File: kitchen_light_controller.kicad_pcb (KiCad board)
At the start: 2 copper layers, 48 x 57 mm, 9 parts, among them J1 1935161, J2 1935161, J3 1935161, J4 1935161, J5 1935161, U1 SC0915, U2 VND7140AJTR, U3 VND7140AJTR

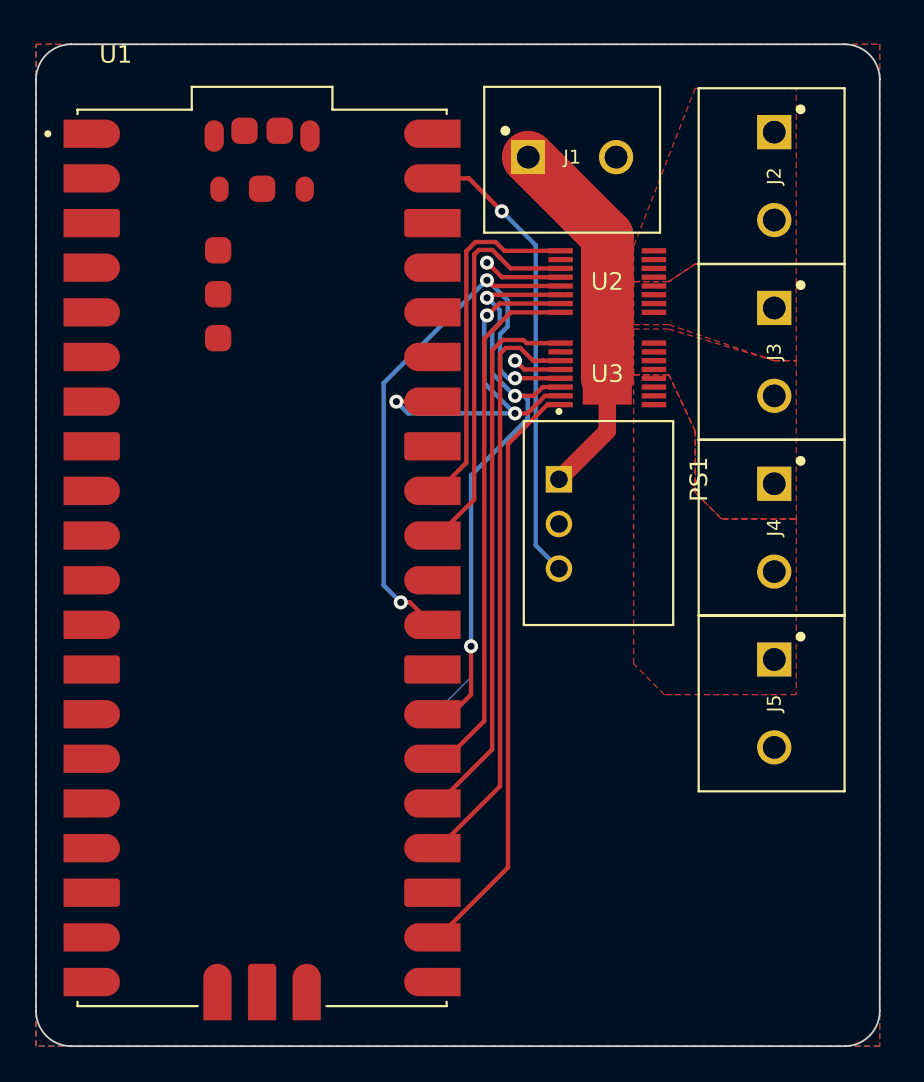
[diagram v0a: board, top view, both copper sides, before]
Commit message: Reduced to dual channel (Single IC)
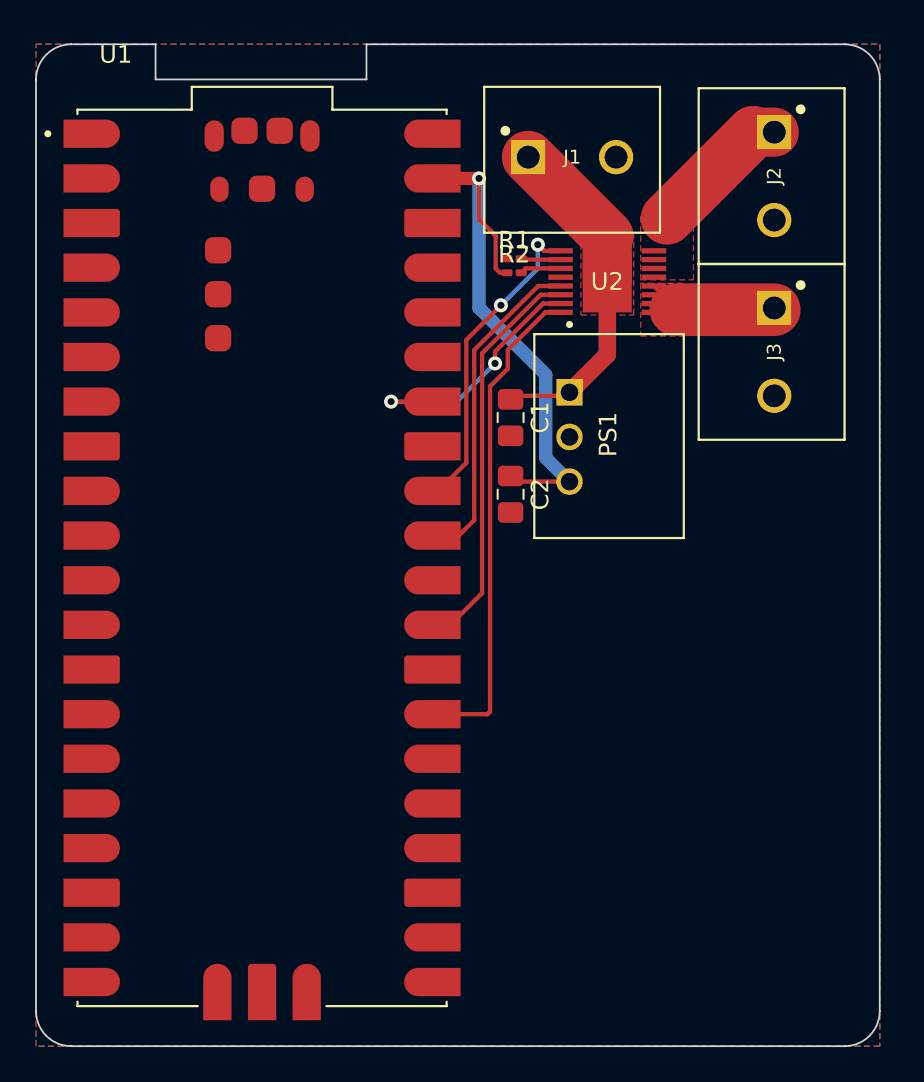
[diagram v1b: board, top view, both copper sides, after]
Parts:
- removed J4, J5: 1935161, Raspberry Pi Pico:PHOENIX_1935161
- removed U3: VND7140AJTR, Raspberry Pi Pico:POWERSSO16_STM
- added C1: 10μF, Capacitor_SMD:C_0805_2012Metric_Pad1.18x1.45mm_HandSolder, F.Cu at (103.0, 50.2)
- added C2: 10μF, Capacitor_SMD:C_0805_2012Metric_Pad1.18x1.45mm_HandSolder, F.Cu at (103.0, 54.6)
- added R1: 15KΩ, Resistor_SMD:R_0201_0603Metric_Pad0.64x0.40mm_HandSolder, F.Cu at (103.2, 41.2)
- added R2: 15KΩ, Resistor_SMD:R_0201_0603Metric_Pad0.64x0.40mm_HandSolder, F.Cu at (103.2, 42.0)
- moved PS1 4.99 mm to (108.6, 51.3)
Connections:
- U1 pad 22: PWM3 -> unconnected-(U1-GP17-Pad22)
- U1 pad 24: MS_CE1 -> unconnected-(U1-GP18-Pad24)
- U1 pad 25: PWM2 -> unconnected-(U1-GP19-Pad25)
- U1 pad 26: PWM1 -> unconnected-(U1-GP20-Pad26)
- U1 pad 27: MS_SEL1 -> PWM1
- U1 pad 29: MS_SEL0 -> MS_SEL1
- U1 pad 31: MS_CE0 -> MS_SEL0
- U2 pad 2: unconnected-(U2-*FAULTRST-Pad2) -> Net-(U2-*FAULTRST)
- U2 pad 3: MS_CE0 -> Net-(U2-SEN)
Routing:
- net PWM3: track 34.0 -> 0.00 mm
- net MS_CE1: track 33.8 -> 0.00 mm
- net PWM2: track 31.6 -> 0.00 mm
- net MS_CE0: track 22.6 -> 0.00 mm
- net MS_SEL0: track 37.3 -> 18.8 mm, vias 3 -> 0
- net MS_SEL1: track 40.1 -> 23.1 mm, vias 3 -> 0
- net MULTISENSE: track 23.0 -> 14.7 mm, vias 3 -> 2
- net Net-(J2-Pad1): track 0.00 -> 8.13 mm
- net 3.3V: track 26.4 -> 34.4 mm
- net Net-(J3-Pad1): track 0.00 -> 7.36 mm
- net GND: track 7.34 -> 0.00 mm, vias 2 -> 0
- net VIN: track 22.3 -> 19.7 mm
- net Net-(U2-SEN): track 0.00 -> 2.34 mm
- net PWM1: track 30.6 -> 28.2 mm
- net PWM0: track 20.4 -> 18.1 mm, vias 0 -> 2
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- added copper zone on F.Cu, net VIN
- removed copper zone on F.Cu, net Net-(J4-Pad1)
- removed copper zone on F.Cu, net Net-(J5-Pad1)
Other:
- outline, holes or cut-outs redrawn

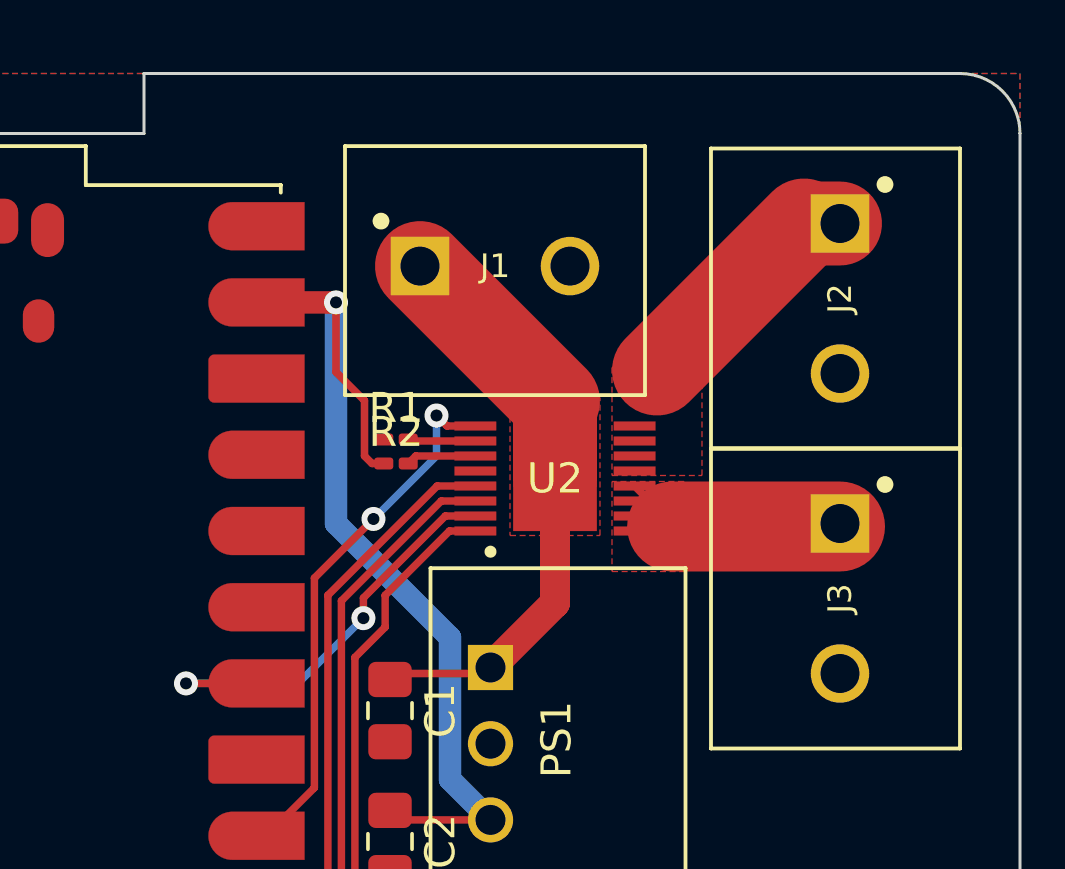
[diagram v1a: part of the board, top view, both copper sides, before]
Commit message: Reinforced current carrying traces with vias
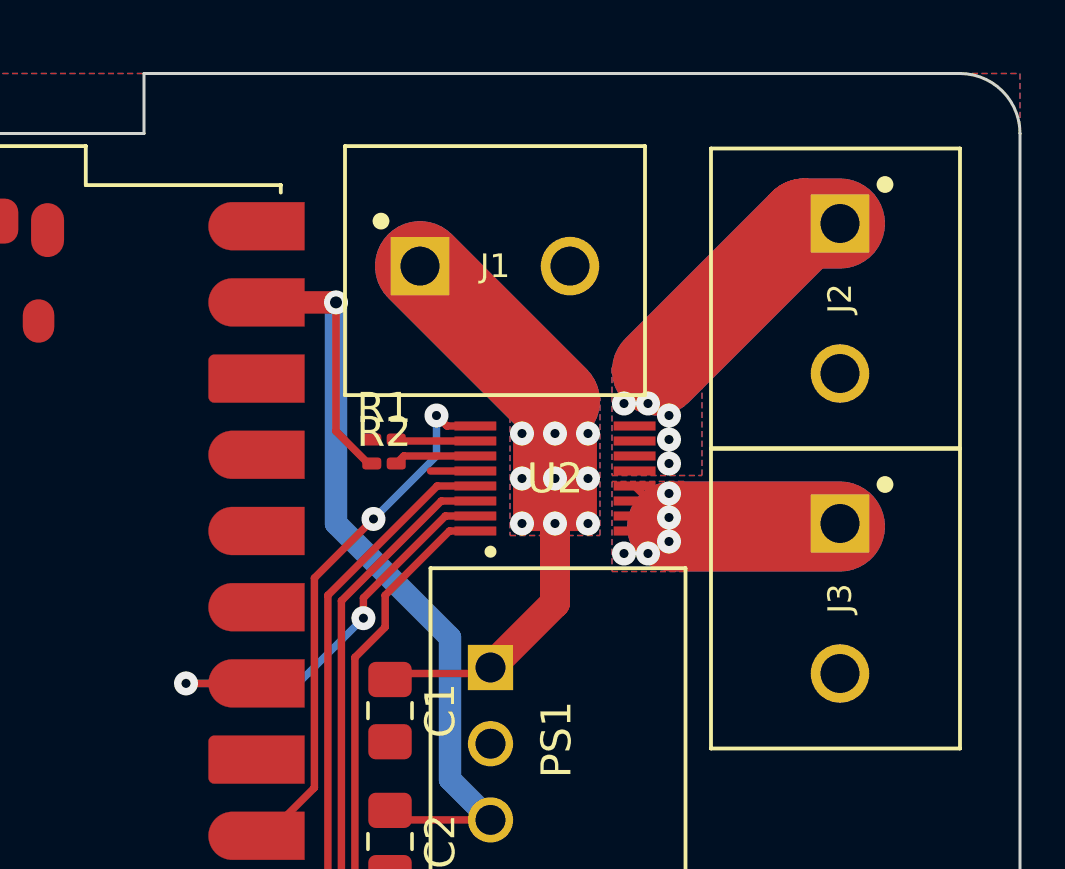
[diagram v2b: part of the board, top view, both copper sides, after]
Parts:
- moved R1 0.40 mm to (102.8, 41.2)
- moved R2 0.40 mm to (102.8, 42.0)
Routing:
- net Net-(J2-Pad1): track 8.13 -> 16.3 mm, vias 0 -> 5
- net Net-(J3-Pad1): track 7.36 -> 13.0 mm, vias 0 -> 5
- net VIN: track 19.7 -> 23.4 mm, vias 0 -> 9
- net GND: track 0.00 -> 1.50 mm
- added copper zone on B.Cu, net Net-(J2-Pad1)
- added copper zone on B.Cu, net Net-(J3-Pad1)
- added copper zone on B.Cu, net VIN
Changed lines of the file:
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@@
   (net 49 "MULTISENSE")
   (footprint "Resistor_SMD:R_0201_0603Metric_Pad0.64x0.40mm_HandSolder" (layer "F.Cu")
-    (at 103.2 41.2)
+    (at 102.8 41.2)
     (descr "Resistor SMD 0201 (0603 Metric), square (rectangular) end terminal, IPC_7351 nominal with elongated pad for handsoldering. (Body size source: https://www.vishay.com/docs/20052/crcw0201e3.pdf), generated with kicad-footprint-generator")
     (tags "resistor handsolder")
@@
   )
   (footprint "Resistor_SMD:R_0201_0603Metric_Pad0.64x0.40mm_HandSolder" (layer "F.Cu")
-    (at 103.2 42)
+    (at 102.8 42)
     (descr "Resistor SMD 0201 (0603 Metric), square (rectangular) end terminal, IPC_7351 nominal with elongated pad for handsoldering. (Body size source: https://www.vishay.com/docs/20052/crcw0201e3.pdf), generated with kicad-footprint-generator")
     (tags "resistor handsolder")
@@
   (segment (start 103 49.2) (end 103.2 49) (width 0.25) (layer "F.Cu") (net 1))
   (segment (start 103.2 49) (end 106.15 49) (width 0.25) (layer "F.Cu") (net 1))
-  (segment (start 108.5 39.92) (end 108.5 42.5) (width 2.8) (layer "F.Cu") (net 1))
   (segment (start 108.5 46.65) (end 108.5 42.5) (width 1) (layer "F.Cu") (net 1))
   (segment (start 104 35.42) (end 108.5 39.92) (width 3) (layer "F.Cu") (net 1))
   (segment (start 106.15 49) (end 106.35 48.8) (width 0.25) (layer "F.Cu") (net 1))
   (segment (start 106.35 48.8) (end 108.5 46.65) (width 1) (layer "F.Cu") (net 1))
-  (segment (start 118 34) (end 116.8 34) (width 2.8) (layer "F.Cu") (net 3))
+  (via (at 107.4 42.5) (size 0.8) (drill 0.3) (layers "F.Cu" "B.Cu") (net 1))
+  (via (at 109.6 42.5) (size 0.8) (drill 0.3) (layers "F.Cu" "B.Cu") (net 1))
+  (via (at 109.6 41) (size 0.8) (drill 0.3) (layers "F.Cu" "B.Cu") (net 1))
+  (via (at 108.5 41) (size 0.8) (drill 0.3) (layers "F.Cu" "B.Cu") (net 1))
+  (via (at 109.6 44) (size 0.8) (drill 0.3) (layers "F.Cu" "B.Cu") (net 1))
+  (via (at 108.5 42.5) (size 0.8) (drill 0.3) (layers "F.Cu" "B.Cu") (net 1))
+  (via (at 108.5 44) (size 0.8) (drill 0.3) (layers "F.Cu" "B.Cu") (net 1))
+  (via (at 107.4 41) (size 0.8) (drill 0.3) (layers "F.Cu" "B.Cu") (net 1))
+  (via (at 107.4 44) (size 0.8) (drill 0.3) (layers "F.Cu" "B.Cu") (net 1))
+  (segment (start 104 35.42) (end 108.5 39.92) (width 3) (layer "B.Cu") (net 1))
+  (segment (start 105.8457 42.249937) (end 104.350063 42.249937) (width 0.25) (layer "F.Cu") (net 2))
+  (segment (start 118 34) (end 116.8 34) (width 3) (layer "F.Cu") (net 3))
   (segment (start 116.8 34) (end 111.9 38.9) (width 3) (layer "F.Cu") (net 3))
-  (segment (start 101.2 38.95331) (end 102.15 39.90331) (width 0.25) (layer "F.Cu") (net 4))
+  (via (at 110.8 40) (size 0.8) (drill 0.3) (layers "F.Cu" "B.Cu") (free) (net 3))
+  (via (at 112.3 40.4) (size 0.8) (drill 0.3) (layers "F.Cu" "B.Cu") (free) (net 3))
+  (via (at 112.3 41.2) (size 0.8) (drill 0.3) (layers "F.Cu" "B.Cu") (free) (net 3))
+  (via (at 112.3 42) (size 0.8) (drill 0.3) (layers "F.Cu" "B.Cu") (free) (net 3))
+  (via (at 111.6 40) (size 0.8) (drill 0.3) (layers "F.Cu" "B.Cu") (free) (net 3))
+  (segment (start 118 34) (end 116.8 34) (width 3) (layer "B.Cu") (net 3))
+  (segment (start 116.8 34) (end 111.9 38.9) (width 3) (layer "B.Cu") (net 3))
   (segment (start 101.2 36.63) (end 98.58 36.63) (width 0.75) (layer "F.Cu") (net 4))
+  (segment (start 102.273959 42) (end 102.3925 42) (width 0.25) (layer "F.Cu") (net 4))
   (segment (start 98.55 36.63) (end 101.2 36.63) (width 0.25) (layer "F.Cu") (net 4))
-  (segment (start 102.15 39.90331) (end 102.15 41.75) (width 0.25) (layer "F.Cu") (net 4))
-  (segment (start 101.2 36.63) (end 101.2 38.95331) (width 0.25) (layer "F.Cu") (net 4))
   (segment (start 98.58 36.6) (end 98.55 36.63) (width 0.25) (layer "F.Cu") (net 4))
-  (segment (start 102.15 41.75) (end 102.4 42) (width 0.25) (layer "F.Cu") (net 4))
-  (segment (start 102.4 42) (end 102.7925 42) (width 0.25) (layer "F.Cu") (net 4))
   (segment (start 103 53.5625) (end 103.3175 53.88) (width 0.25) (layer "F.Cu") (net 4))
   (segment (start 103.3175 53.88) (end 106.35 53.88) (width 0.25) (layer "F.Cu") (net 4))
+  (segment (start 101.2 40.926041) (end 102.273959 42) (width 0.25) (layer "F.Cu") (net 4))
+  (segment (start 101.2 36.63) (end 101.2 40.926041) (width 0.25) (layer "F.Cu") (net 4))
   (via (at 101.2 36.63) (size 0.8) (drill 0.4) (layers "F.Cu" "B.Cu") (free) (net 4))
   (segment (start 105 47.8) (end 105 52.53) (width 0.75) (layer "B.Cu") (net 4))
@@
   (segment (start 112.404237 44) (end 111.1543 42.750063) (width 0.25) (layer "F.Cu") (net 24))
   (segment (start 112.404237 44.1) (end 118 44.1) (width 3) (layer "F.Cu") (net 24))
-  (segment (start 105.8457 41.249685) (end 103.657185 41.249685) (width 0.25) (layer "F.Cu") (net 32))
-  (segment (start 103.657185 41.249685) (end 103.6075 41.2) (width 0.25) (layer "F.Cu") (net 32))
-  (segment (start 103.857689 41.749811) (end 103.6075 42) (width 0.25) (layer "F.Cu") (net 33))
-  (segment (start 105.8457 41.749811) (end 103.857689 41.749811) (width 0.25) (layer "F.Cu") (net 33))
+  (via (at 111.6 45) (size 0.8) (drill 0.3) (layers "F.Cu" "B.Cu") (free) (net 24))
+  (via (at 112.3 43.8) (size 0.8) (drill 0.3) (layers "F.Cu" "B.Cu") (free) (net 24))
+  (via (at 112.3 44.6) (size 0.8) (drill 0.3) (layers "F.Cu" "B.Cu") (free) (net 24))
+  (via (at 110.8 45) (size 0.8) (drill 0.3) (layers "F.Cu" "B.Cu") (free) (net 24))
+  (via (at 112.3 43) (size 0.8) (drill 0.3) (layers "F.Cu" "B.Cu") (free) (net 24))
+  (segment (start 112.402118 44.1) (end 117.997881 44.1) (width 3) (layer "B.Cu") (net 24))
+  (segment (start 103.257185 41.249685) (end 103.2075 41.2) (width 0.25) (layer "F.Cu") (net 32))
+  (segment (start 105.8457 41.249685) (end 103.257185 41.249685) (width 0.25) (layer "F.Cu") (net 32))
+  (segment (start 103.457689 41.749811) (end 103.2075 42) (width 0.25) (layer "F.Cu") (net 33))
+  (segment (start 105.8457 41.749811) (end 103.457689 41.749811) (width 0.25) (layer "F.Cu") (net 33))
   (segment (start 105.8457 44.250441) (end 104.981196 44.250441) (width 0.25) (layer "F.Cu") (net 34))
   (segment (start 102.838566 46.393071) (end 102.838566 47.455862) (width 0.25) (layer "F.Cu") (net 34))
@@
   (segment (start 104.549559 40.4) (end 104.899118 40.749559) (width 0.25) (layer "F.Cu") (net 48))
   (segment (start 104.899118 40.749559) (end 105.8457 40.749559) (width 0.25) (layer "F.Cu") (net 48))
-  (via (at 102.448925 43.848925) (size 0.8) (drill 0.4) (layers "F.Cu" "B.Cu") (free) (net 48))
-  (via (at 104.549559 40.4) (size 0.8) (drill 0.4) (layers "F.Cu" "B.Cu") (free) (net 48))
+  (via (at 102.448925 43.848925) (size 0.8) (drill 0.3) (layers "F.Cu" "B.Cu") (free) (net 48))
+  (via (at 104.549559 40.4) (size 0.8) (drill 0.3) (layers "F.Cu" "B.Cu") (free) (net 48))
   (segment (start 104.549559 41.748291) (end 104.549559 40.4) (width 0.25) (layer "B.Cu") (net 48))
   (segment (start 102.448925 43.848925) (end 104.549559 41.748291) (width 0.25) (layer "B.Cu") (net 48))
@@
   (segment (start 96.2 49.33) (end 98.55 49.33) (width 0.25) (layer "F.Cu") (net 49))
   (segment (start 102.113566 46.481675) (end 104.844926 43.750315) (width 0.25) (layer "F.Cu") (net 49))
-  (via (at 96.2 49.33) (size 0.8) (drill 0.4) (layers "F.Cu" "B.Cu") (free) (net 49))
-  (via (at 102.113566 47.155557) (size 0.8) (drill 0.4) (layers "F.Cu" "B.Cu") (free) (net 49))
+  (via (at 96.2 49.33) (size 0.8) (drill 0.3) (layers "F.Cu" "B.Cu") (free) (net 49))
+  (via (at 102.113566 47.155557) (size 0.8) (drill 0.3) (layers "F.Cu" "B.Cu") (free) (net 49))
   (segment (start 102.113566 47.155557) (end 99.939123 49.33) (width 0.25) (layer "B.Cu") (net 49))
   (segment (start 99.939123 49.33) (end 96.2 49.33) (width 0.25) (layer "B.Cu") (net 49))
-  (zone (net 1) (net_name "VIN") (layer "F.Cu") (hatch edge 0.5)
+  (zone (net 2) (net_name "GND") (layers "F&B.Cu") (name "GroundPlane") (hatch edge 0.5)
+    (connect_pads (clearance 0.25))
+    (min_thickness 0.25) (filled_areas_thickness no)
+    (fill yes (thermal_gap 0.5) (thermal_bridge_width 0.5) (island_removal_mode 1) (island_area_min 10))
+    (polygon
+      (pts
+        (xy 76 29)
+        (xy 124 29)
+        (xy 124 86)
+        (xy 76 86)
+      )
+    )
+  )
+  (zone (net 1) (net_name "VIN") (layers "F&B.Cu") (hatch edge 0.5)
     (priority 3)
     (connect_pads yes (clearance 0))
@@
     )
   )
-  (zone (net 3) (net_name "Net-(J2-Pad1)") (layer "F.Cu") (hatch edge 0.5)
+  (zone (net 3) (net_name "Net-(J2-Pad1)") (layers "F&B.Cu") (hatch edge 0.5)
     (priority 2)
     (connect_pads yes (clearance 0))
@@
     )
   )
-  (zone (net 24) (net_name "Net-(J3-Pad1)") (layer "F.Cu") (hatch edge 0.5)
+  (zone (net 24) (net_name "Net-(J3-Pad1)") (layers "F&B.Cu") (hatch edge 0.5)
     (priority 1)
     (connect_pads yes (clearance 0))
@@
       )
     )
-  )
-  (zone (net 2) (net_name "GND") (layers "F&B.Cu") (name "GroundPlane") (hatch edge 0.5)
-    (connect_pads (clearance 0.25))
-    (min_thickness 0.25) (filled_areas_thickness no)
-    (fill yes (thermal_gap 0.5) (thermal_bridge_width 0.5) (island_removal_mode 1) (island_area_min 10))
-    (polygon
-      (pts
-        (xy 76 29)
-        (xy 124 29)
-        (xy 124 86)
-        (xy 76 86)
-      )
-    )
